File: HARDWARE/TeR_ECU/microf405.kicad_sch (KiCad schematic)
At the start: 25 parts, among them J1 FTSH-105-01-L-DV-K-TR, SW1 RST, U6 STM32F405VGTx, X2 ASE-xxxMHz

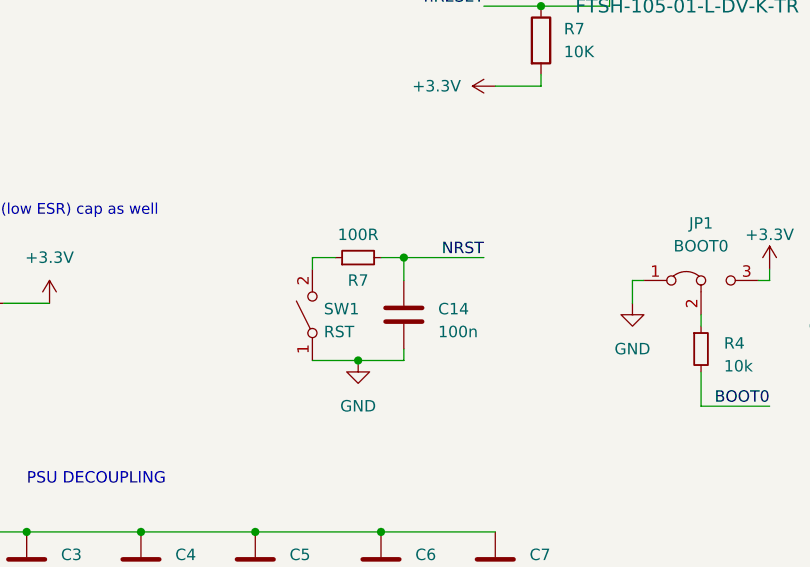
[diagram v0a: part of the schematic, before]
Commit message: nrst doesnt need ressistance
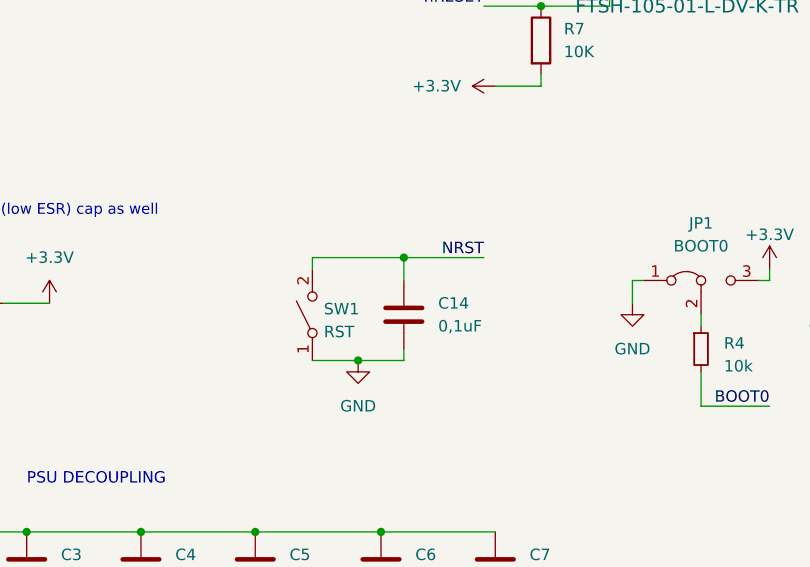
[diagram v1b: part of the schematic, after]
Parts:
- removed R7: 100R, Resistor_SMD:R_0603_1608Metric, symbol Device:R_Small
- C14: value 100n -> 0,1uF
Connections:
- net NRST: now also SW1.2 (B)
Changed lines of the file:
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@@
-    (stroke (width 0) (type default))
-  )
-  (wire (pts (xy 93.98 134.62) (xy 96.52 134.62))
     (stroke (width 0) (type default))
   )
@@
     (stroke (width 0) (type default))
   )
-  (wire (pts (xy 101.6 134.62) (xy 104.14 134.62))
+  (wire (pts (xy 93.98 134.62) (xy 104.14 134.62))
     (stroke (width 0) (type default))
   )
@@
   (symbol (lib_id "Device:C") (at 104.14 140.97 0) (unit 1)
     (in_bom yes) (on_board yes) (dnp no) (fields_autoplaced)
-    (property "Reference" "C14" (at 107.95 140.335 0)
-      (effects (font (size 1.27 1.27)) (justify left))
-    )
-    (property "Value" "100n" (at 107.95 142.875 0)
+    (property "Reference" "C14" (at 107.95 139.7 0)
+      (effects (font (size 1.27 1.27)) (justify left))
+    )
+    (property "Value" "0,1uF" (at 107.95 142.24 0)
       (effects (font (size 1.27 1.27)) (justify left))
     )
@@
         )
       )
-    )
-  )
-  (symbol (lib_id "Device:R_Small") (at 99.06 134.62 90) (unit 1)
-    (in_bom yes) (on_board yes) (dnp no)
-    (property "Reference" "R7" (at 99.06 137.16 90)
-      (effects (font (size 1.27 1.27)))
-    )
-    (property "Value" "100R" (at 99.06 132.08 90)
-      (effects (font (size 1.27 1.27)))
-    )
-    (property "Footprint" "Resistor_SMD:R_0603_1608Metric" (at 99.06 134.62 0)
-      (effects (font (size 1.27 1.27)) hide)
-    )
-    (property "Datasheet" "~" (at 99.06 134.62 0)
-      (effects (font (size 1.27 1.27)) hide)
-    )
-    (pin "1")
-    (pin "2")
-    (instances
-      (project "TER_PEDAL"
-        (path "/73ede3a3-6344-40fe-9207-10ff50d388ba/7632a94a-0691-4527-83e2-6d814eae7e64"
-          (reference "R7") (unit 1)
-        )
-      )
-      (project "TeR_ECU"
-        (path "/84413845-c4f3-4743-bcd2-a67649c90902/6cf54a6a-28e2-462f-b0c6-d7147ca367a6"
-          (reference "R2") (unit 1)
-        )
-      )
-      (project "TeR_FrontAxle"
-        (path "/8643b8d3-2324-4109-bb49-1b773a0e4e20/e12cc919-5cc0-4c25-902e-c831d62c95af"
-          (reference "R2") (unit 1)
-        )
-      )

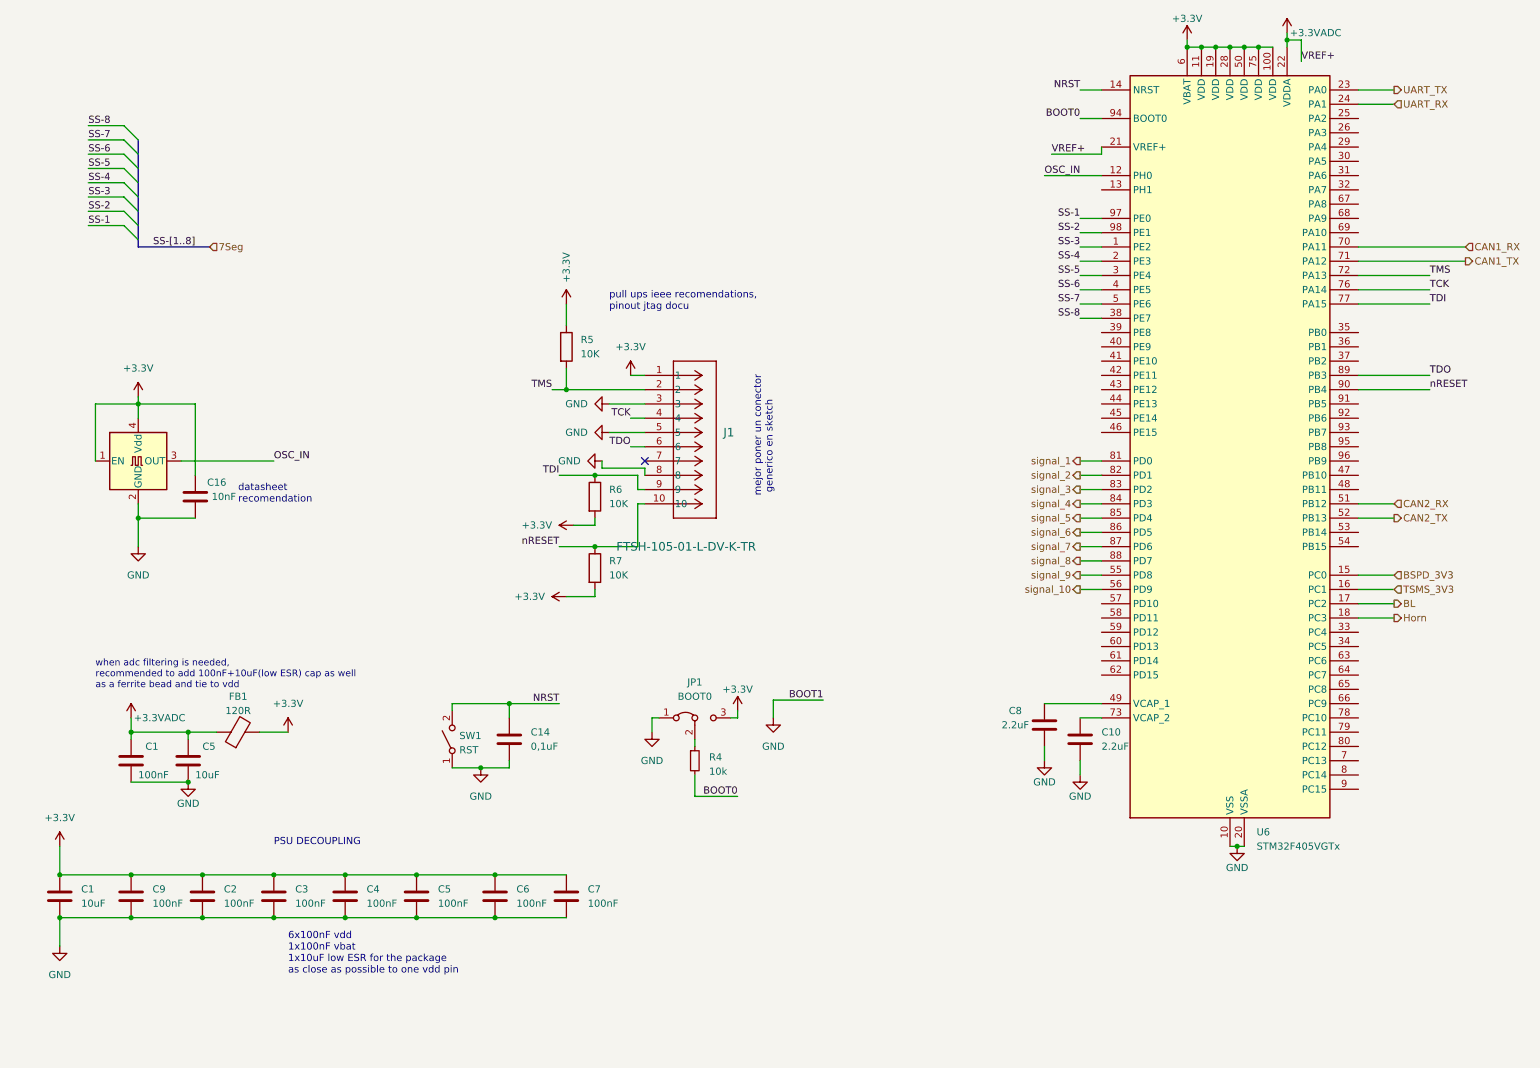
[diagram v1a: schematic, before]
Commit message: idea de esquema de safety y level shifter para señales de 24v
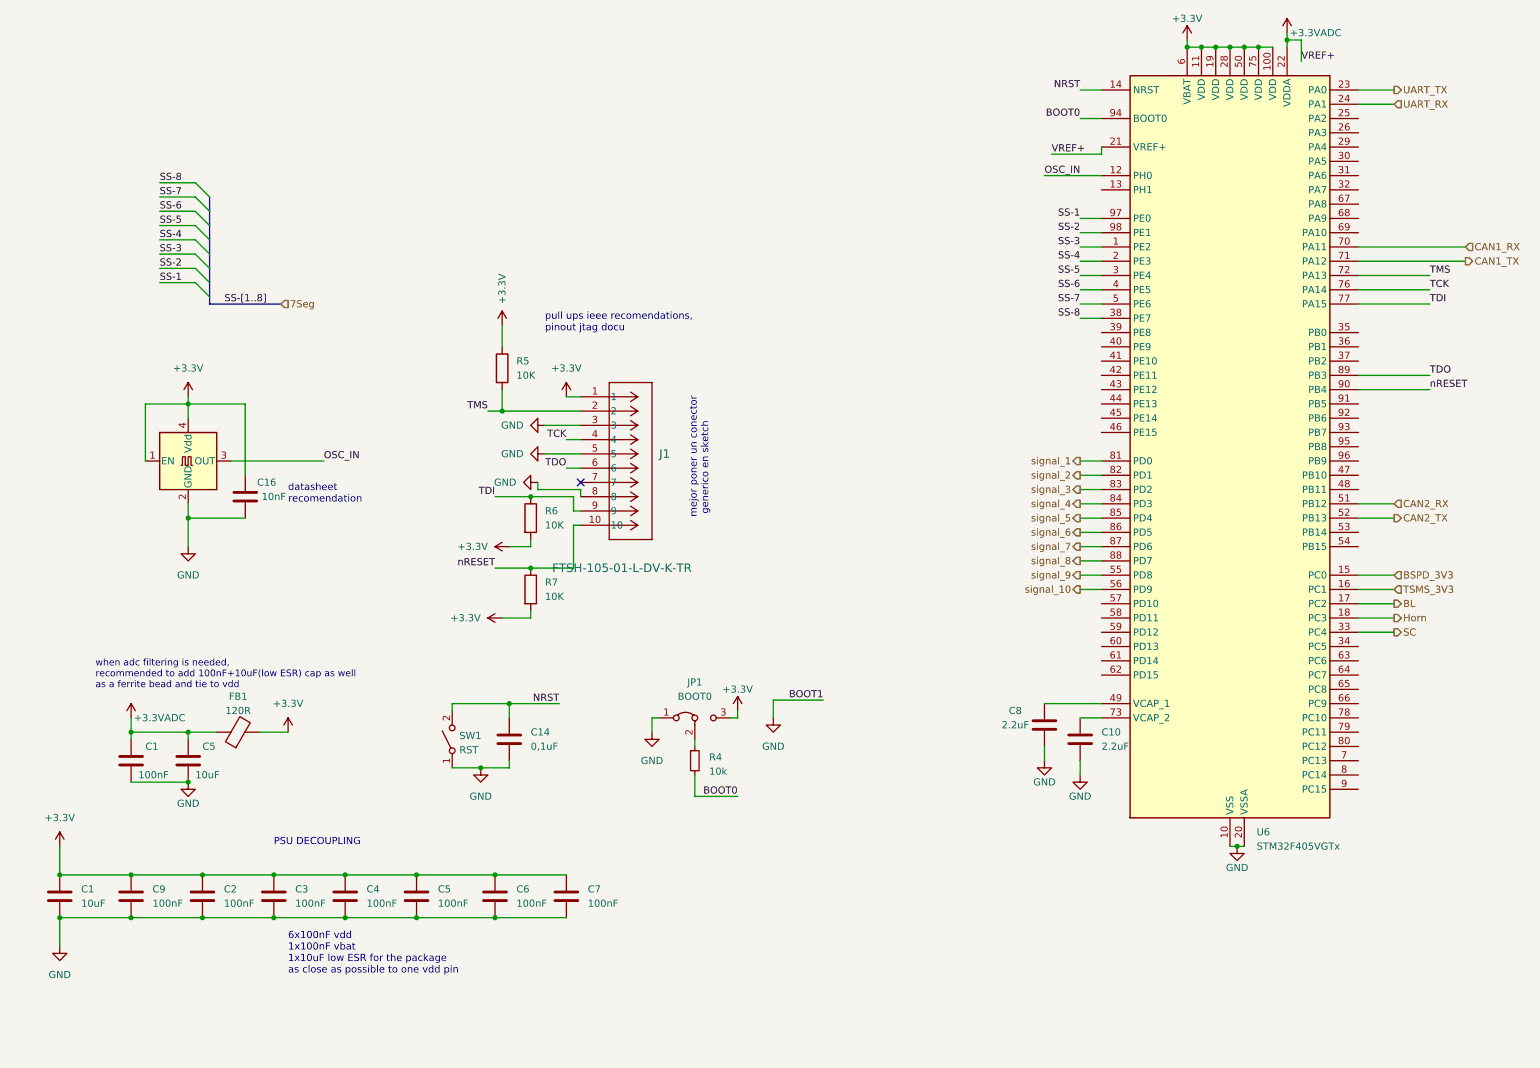
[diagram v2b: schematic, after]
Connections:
- net SC: now reaches U6.33 (PC4)
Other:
- moved on the sheet: C16, J1, R5, R6, R7

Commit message: ic comments
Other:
- moved on the sheet: C16, C8, J1, R5, R6, R7

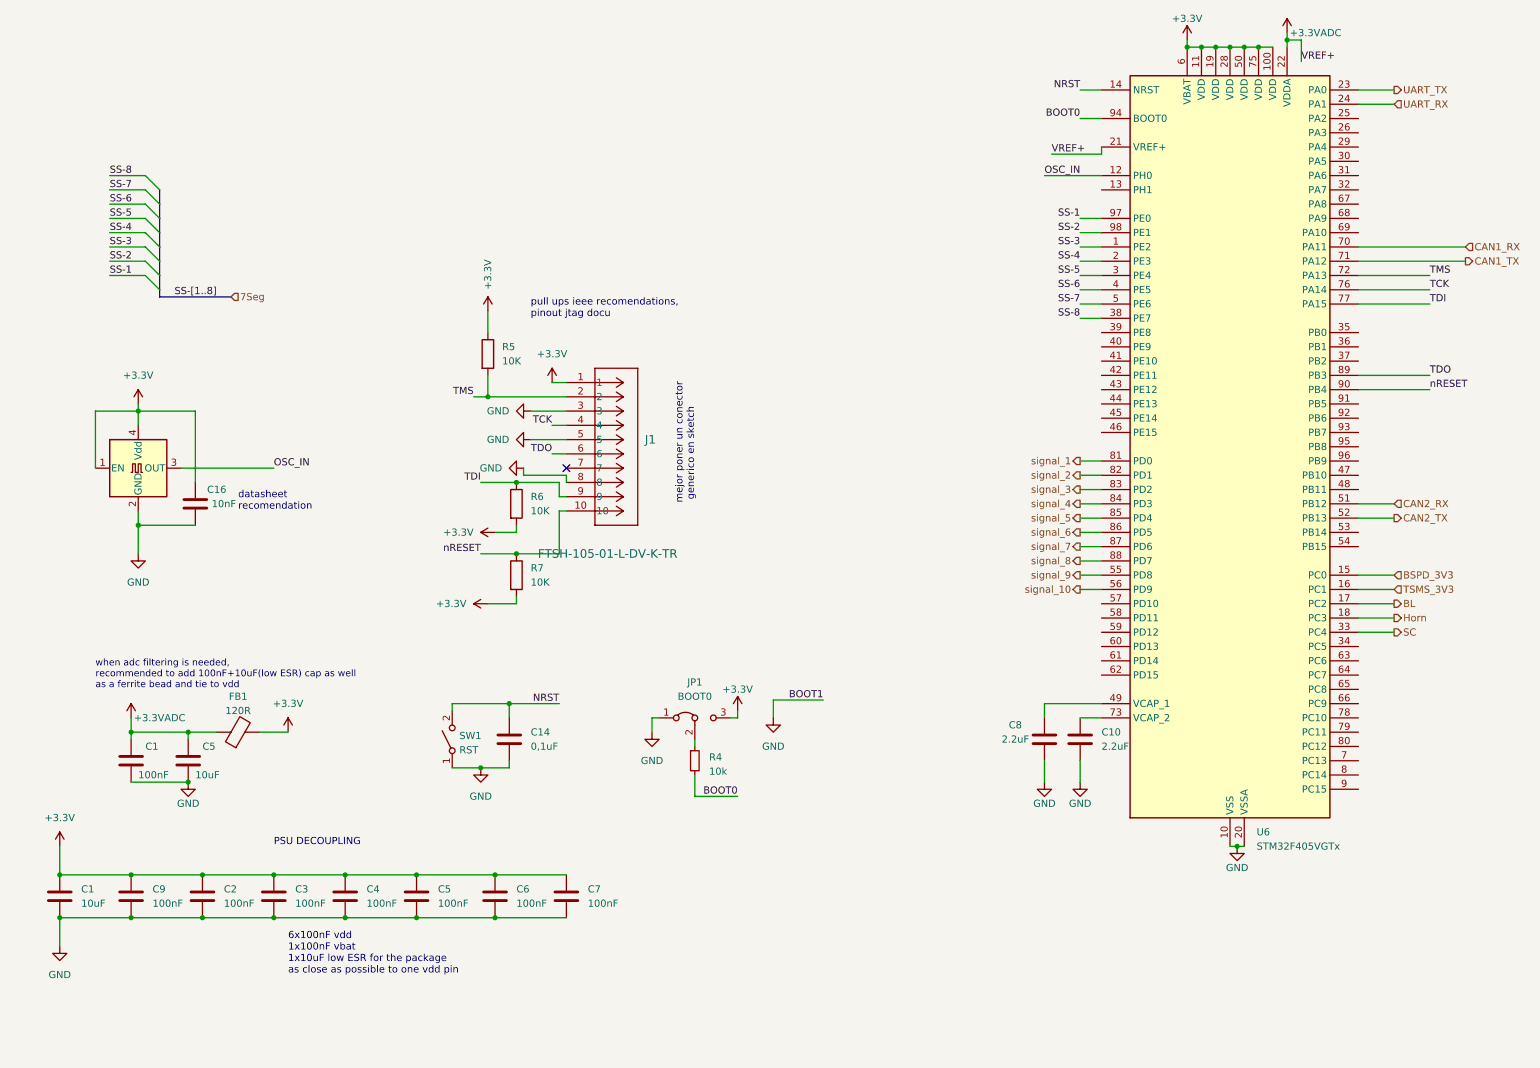
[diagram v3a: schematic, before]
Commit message: sd añadida, uniport redundante eliminado
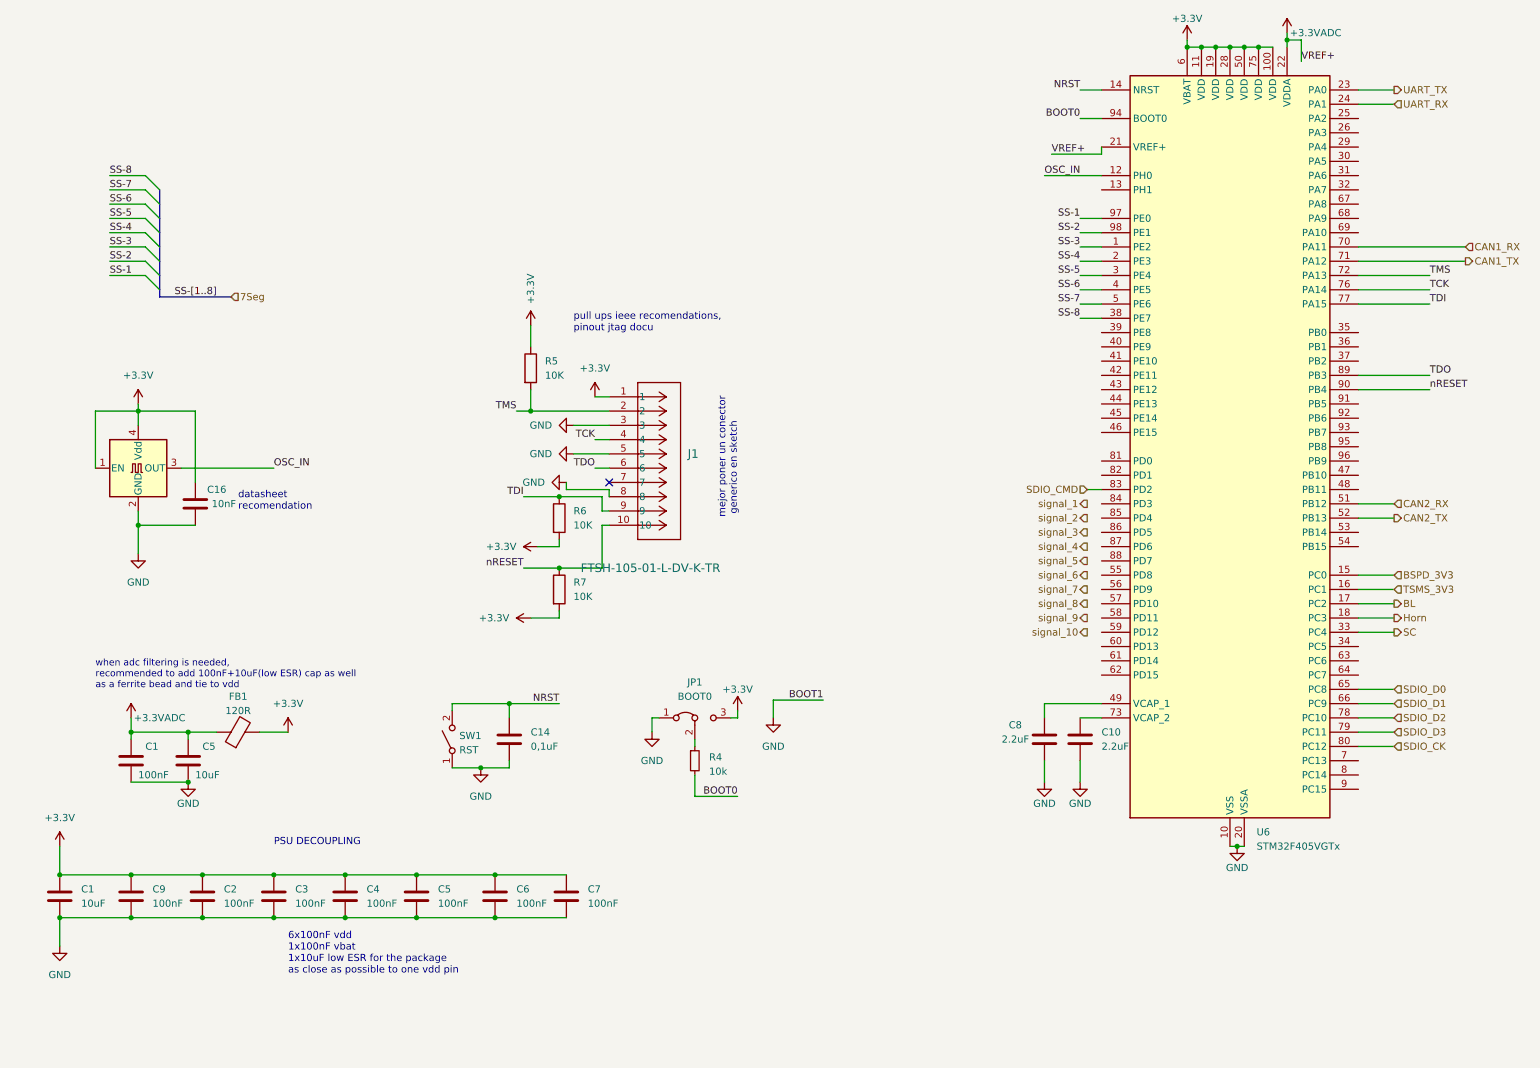
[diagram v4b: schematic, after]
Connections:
- net signal_1: no longer U6.81 (PD0)
- net signal_10: no longer U6.56 (PD9)
- net signal_2: no longer U6.82 (PD1)
- net signal_3: no longer U6.83 (PD2)
- net signal_4: no longer U6.84 (PD3)
- net signal_5: no longer U6.85 (PD4)
- net signal_6: no longer U6.86 (PD5)
- net signal_7: no longer U6.87 (PD6)
- net signal_8: no longer U6.88 (PD7)
- net signal_9: no longer U6.55 (PD8)
- net SDIO_D0: now reaches U6.65 (PC8)
- net SDIO_D1: now reaches U6.66 (PC9)
- net SDIO_D2: now reaches U6.78 (PC10)
- net SDIO_D3: now reaches U6.79 (PC11)
- net SDIO_CK: now reaches U6.80 (PC12)
- new net SDIO_CMD: U6.83 (PD2)
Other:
- moved on the sheet: J1, R5, R6, R7
